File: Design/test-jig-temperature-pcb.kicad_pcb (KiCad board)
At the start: 2 copper layers, 44 parts, among them J1 Jack-DC, J10 Thermistor, J2 SWD, J3 Thermistor, J4 Thermistor, J5 Thermistor, J6 Thermistor, J7 Thermistor, J8 Thermistor, J9 Thermistor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

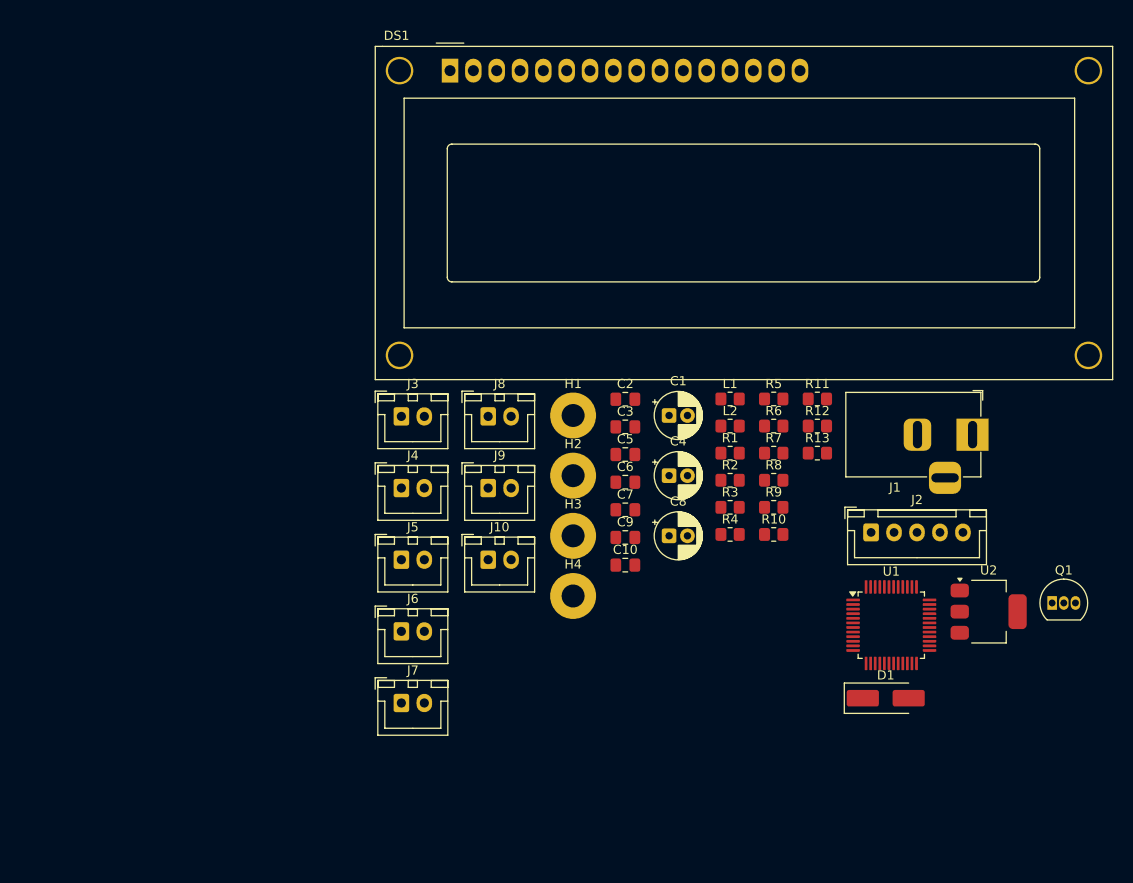
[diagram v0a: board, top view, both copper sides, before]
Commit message: Group components and route thermistor connector to MCU
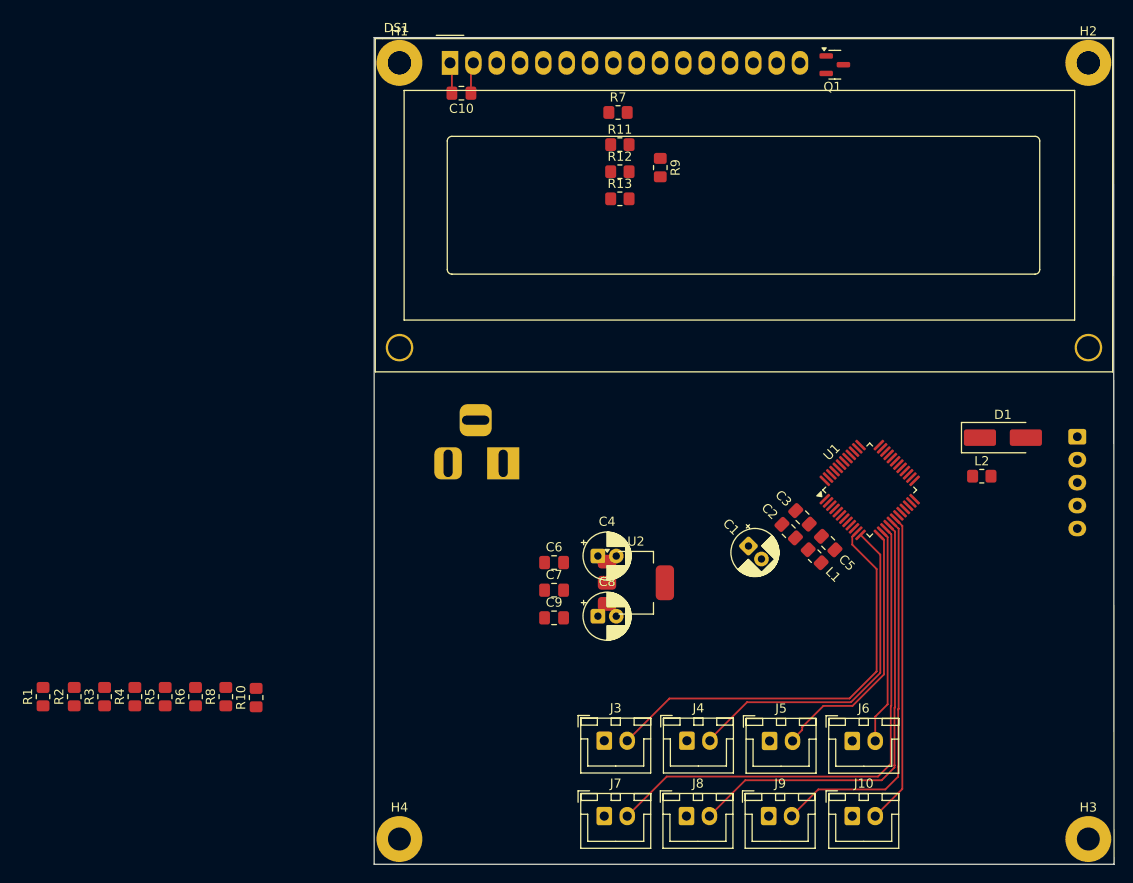
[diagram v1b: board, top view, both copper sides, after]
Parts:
- J1, J2: moved to B.Cu
- Q1: footprint Package_TO_SOT_THT:TO-92_Inline -> Package_TO_SOT_SMD:SOT-23
- moved R1 79.4 mm to (69.1, 132.7), turned to 90 degrees
- moved R2 75.2 mm to (72.5, 132.7), turned to 90 degrees
- moved R5 73.8 mm to (82.4, 132.7), turned to 90 degrees
- moved H2 71.9 mm to (182.9, 63.7)
- moved R3 71.2 mm to (75.8, 132.7), turned to 90 degrees
- moved R6 69.5 mm to (85.7, 132.7), turned to 90 degrees
- moved R4 67.2 mm to (79.1, 132.7), turned to 90 degrees
- moved H3 65.1 mm to (182.9, 148.2)
- moved R8 64.1 mm to (89.0, 132.7), turned to 90 degrees
- moved Q1 63.2 mm to (155.3, 63.9)
- moved R10 59.1 mm to (92.3, 132.8), turned to 90 degrees
- moved C10 54.4 mm to (114.7, 67.0), turned to 180 degrees
- moved J1 51.2 mm to (119.2, 107.3)
- moved J6 50.5 mm to (157.2, 137.5)
- moved J8 48.6 mm to (139.2, 145.7)
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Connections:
- C1 pad 1: Net-(C1-Pad1) -> MCU_VDD
- C2 pad 1: Net-(C1-Pad1) -> MCU_VDD
- C3 pad 1: Net-(C1-Pad1) -> MCU_VDD
- L1 pad 2: Net-(C1-Pad1) -> MCU_VDD
- U1 pad 5: +3.3V -> MCU_VDD
- U1 pad 6: +3.3V -> MCU_VDD
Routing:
- net THERM_5: track 0.00 -> 57.0 mm
- net THERM_6: track 0.00 -> 49.0 mm
- net THERM_1: track 0.00 -> 46.8 mm
- net THERM_7: track 0.00 -> 41.4 mm
- net THERM_2: track 0.00 -> 37.6 mm
- net THERM_8: track 0.00 -> 33.9 mm
- net THERM_3: track 0.00 -> 28.6 mm
- net THERM_4: track 0.00 -> 23.6 mm
- net +5V: track 0.00 -> 3.41 mm
- net GND: track 0.00 -> 3.38 mm
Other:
- board outline added: 80.5 x 90 mm

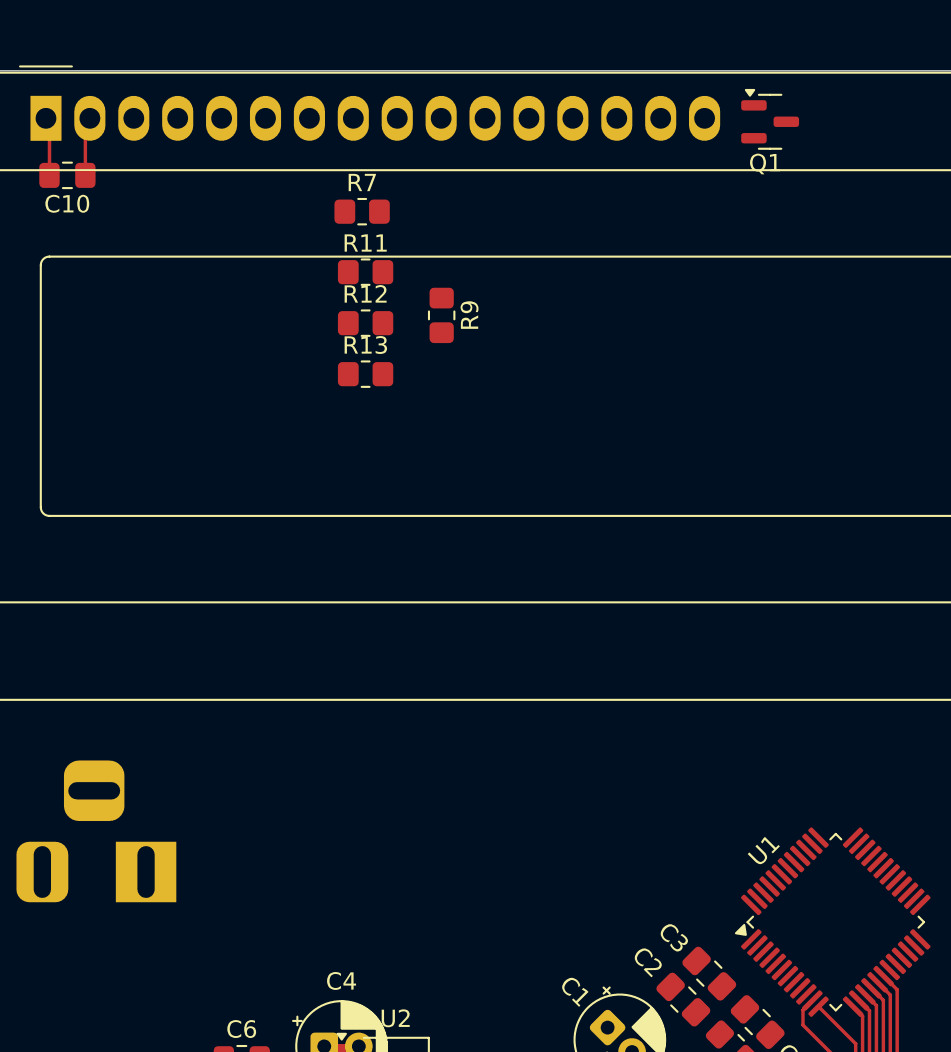
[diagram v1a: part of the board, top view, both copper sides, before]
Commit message: Route the 16x2 LCD to the microcontroller
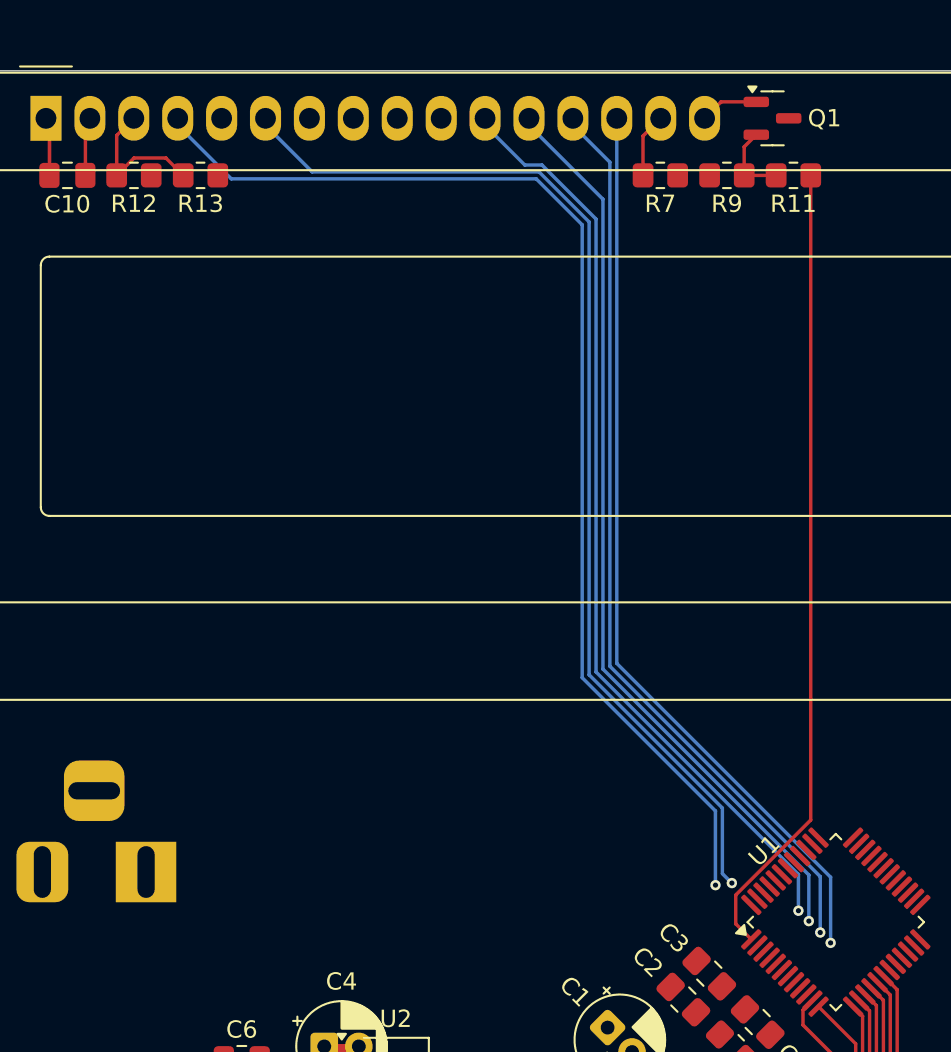
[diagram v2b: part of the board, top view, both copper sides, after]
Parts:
- moved R11 25.4 mm to (156.7, 67.0), turned to 180 degrees
- moved R9 18.4 mm to (152.8, 67.0), turned to 180 degrees
- moved R7 17.4 mm to (148.9, 67.0), turned to 180 degrees
- moved R12 15.9 mm to (118.5, 67.0), turned to 180 degrees
- moved R13 14.9 mm to (122.3, 67.0)
- moved Q1 0.24 mm to (155.4, 63.7)
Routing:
- net LCD_RS: track 0.00 -> 67.6 mm, vias 0 -> 1
- net LCD_EN: track 0.00 -> 63.1 mm, vias 0 -> 1
- net LCD_DATA0: track 0.00 -> 53.9 mm, vias 0 -> 1
- net LCD_DATA1: track 0.00 -> 53.1 mm, vias 0 -> 1
- net LCD_DATA2: track 0.00 -> 53.0 mm, vias 0 -> 1
- net LCD_DATA3: track 0.00 -> 52.8 mm, vias 0 -> 1
- net LCD_BACKLIGHT: track 0.00 -> 46.4 mm
- net Net-(DS1-VO): track 0.00 -> 8.39 mm
- net Net-(Q1-B): track 0.00 -> 4.49 mm
- net Net-(DS1-LED(+)): track 0.00 -> 3.72 mm
- net Net-(DS1-LED(-)): track 0.00 -> 3.38 mm

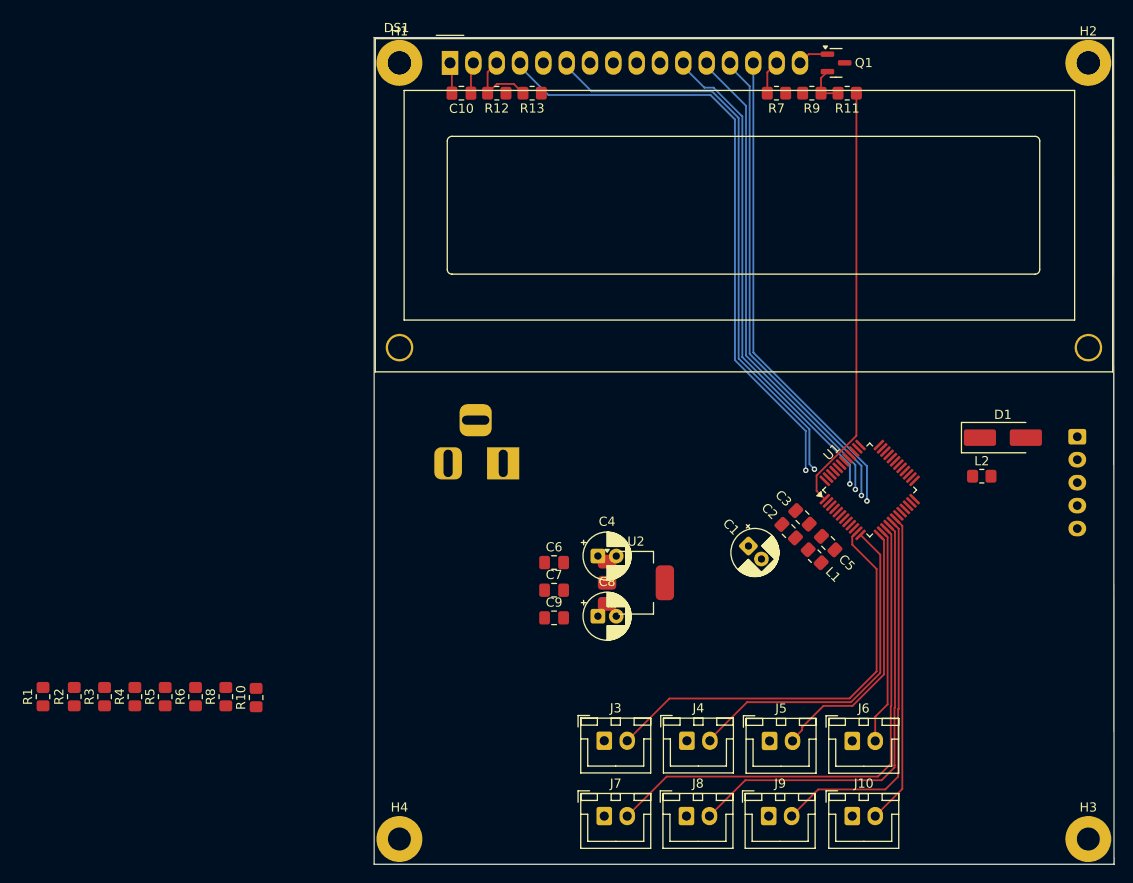
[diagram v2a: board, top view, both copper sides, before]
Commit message: Reposition thermistor connectors and re-route connections
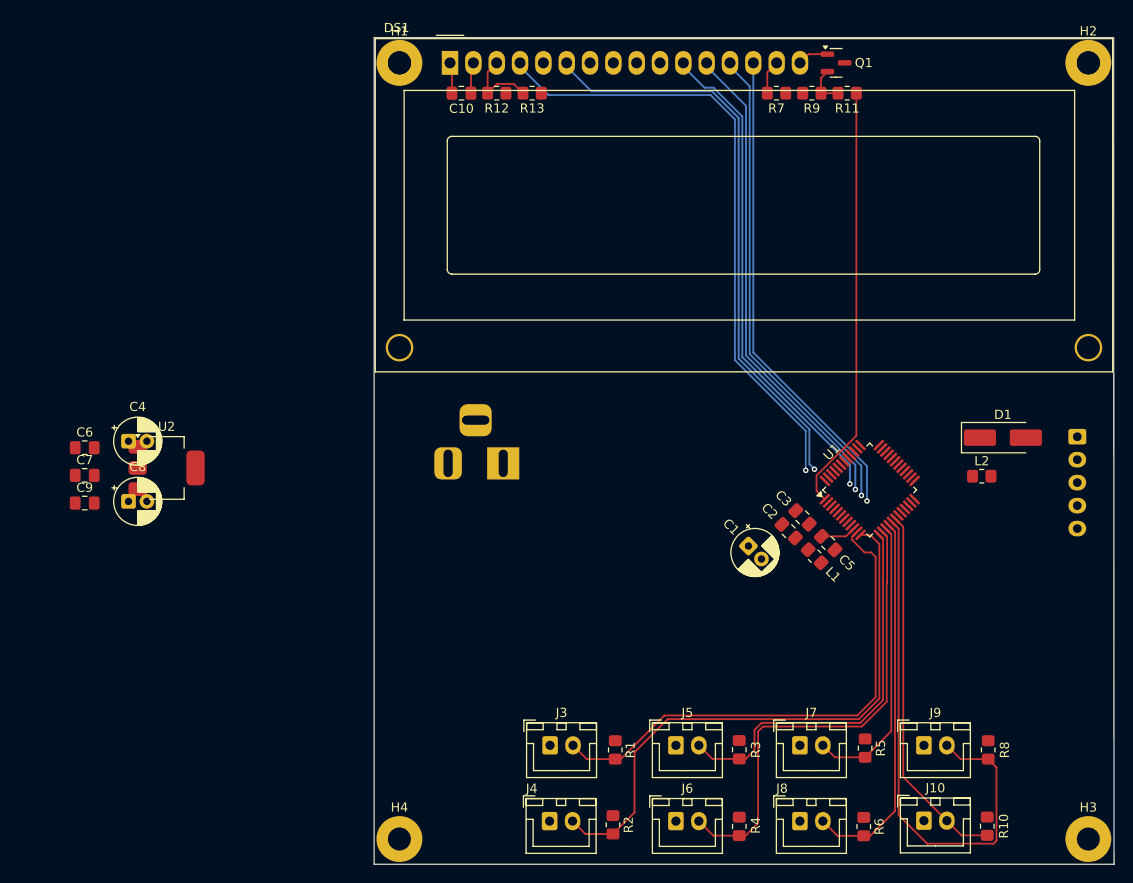
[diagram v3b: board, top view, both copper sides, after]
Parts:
- moved R8 83.2 mm to (172.0, 138.5), turned to -90 degrees
- moved R10 80.8 mm to (171.9, 146.8), turned to -90 degrees
- moved R5 76.4 mm to (158.6, 138.3), turned to -90 degrees
- moved R6 74.1 mm to (158.4, 146.8), turned to -90 degrees
- moved R3 69.3 mm to (144.9, 138.5), turned to -90 degrees
- moved R4 67.3 mm to (144.9, 146.8), turned to -90 degrees
- moved R1 62.6 mm to (131.4, 138.5), turned to -90 degrees
- moved R2 60.3 mm to (131.2, 146.7), turned to -90 degrees
- moved U2 52.6 mm to (82.5, 107.8)
- moved C4 52.6 mm to (78.4, 104.9)
- moved C6 52.6 mm to (73.6, 105.6)
- moved C7 52.6 mm to (73.6, 108.6)
- moved C8 52.6 mm to (78.4, 111.4)
- moved C9 52.6 mm to (73.6, 111.6)
- moved J7 22.6 mm to (151.5, 138.0)
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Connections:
- R1 pad 1: +5V -> +3.3V
- R10 pad 1: +5V -> +3.3V
- R2 pad 1: +5V -> +3.3V
- R3 pad 1: +5V -> +3.3V
- R4 pad 1: +5V -> +3.3V
- R5 pad 1: +5V -> +3.3V
- R6 pad 1: +5V -> +3.3V
- R8 pad 1: +5V -> +3.3V
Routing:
- net THERM_4: track 23.6 -> 51.7 mm
- net THERM_2: track 37.6 -> 63.2 mm
- net THERM_5: track 57.0 -> 31.5 mm
- net THERM_7: track 41.4 -> 58.7 mm
- net THERM_3: track 28.6 -> 42.8 mm
- net THERM_1: track 46.8 -> 56.1 mm
- net THERM_6: track 49.0 -> 41.0 mm
- net THERM_8: track 33.9 -> 40.3 mm
- net SWD_NRST: track 0.00 -> 3.91 mm

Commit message: Route components in power supply section and update README with current PCB image and project structure details
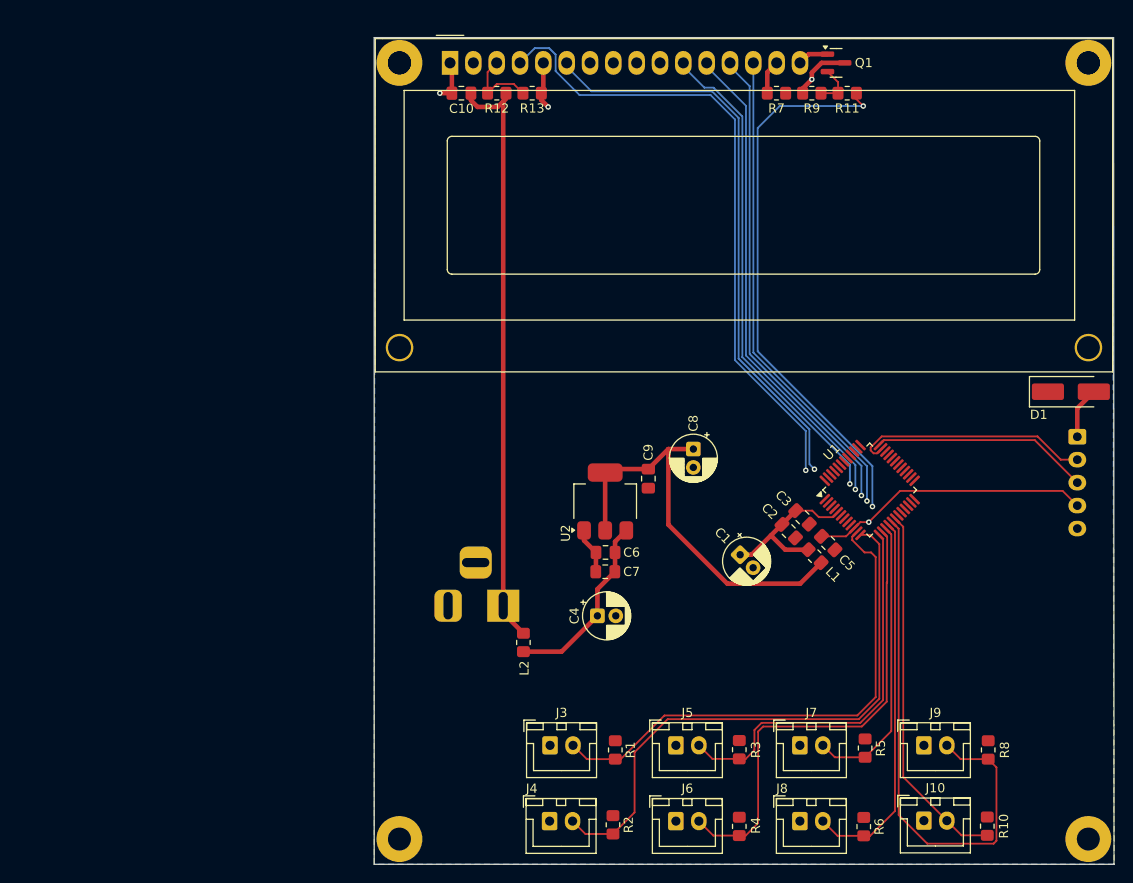
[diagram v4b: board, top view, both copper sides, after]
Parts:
- moved C8 61.8 mm to (139.9, 105.7), turned to -90 degrees
- moved C9 61.4 mm to (135.0, 109.0), turned to -90 degrees
- moved C6 57.8 mm to (130.3, 117.0), turned to 180 degrees
- moved C7 57.6 mm to (130.3, 119.1), turned to 180 degrees
- moved C4 54.5 mm to (129.5, 123.9)
- moved L2 53.1 mm to (121.4, 126.8), turned to -90 degrees
- moved U2 47.9 mm to (130.3, 111.5), turned to 90 degrees
- moved J1 15.5 mm to (119.2, 122.8)
- moved D1 8.93 mm to (181.0, 99.5)
- moved C1 1.31 mm to (145.0, 117.2)
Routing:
- net +5V: track 3.41 -> 65.0 mm
- net +3.3V: track 0.00 -> 45.4 mm
- net SWD_NRST: track 3.91 -> 30.6 mm, vias 0 -> 1
- net SWD_SWDIO: track 0.00 -> 26.0 mm
- net SWD_SWCLK: track 0.00 -> 23.7 mm
- net Net-(U2-VI): track 0.00 -> 20.3 mm
- net GND: track 3.38 -> 21.6 mm, vias 0 -> 3
- net MCU_VDD: track 0.00 -> 17.8 mm
- net LCD_BACKLIGHT: track 46.4 -> 60.6 mm, vias 0 -> 2
- net SWD_+5V: track 0.00 -> 5.65 mm
- net LCD_RS: track 67.6 -> 70.1 mm
- added copper zone on B.Cu, net GND
